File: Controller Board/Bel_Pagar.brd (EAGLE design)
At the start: 7 parts, among them IC1 7805T, Q1 BD140

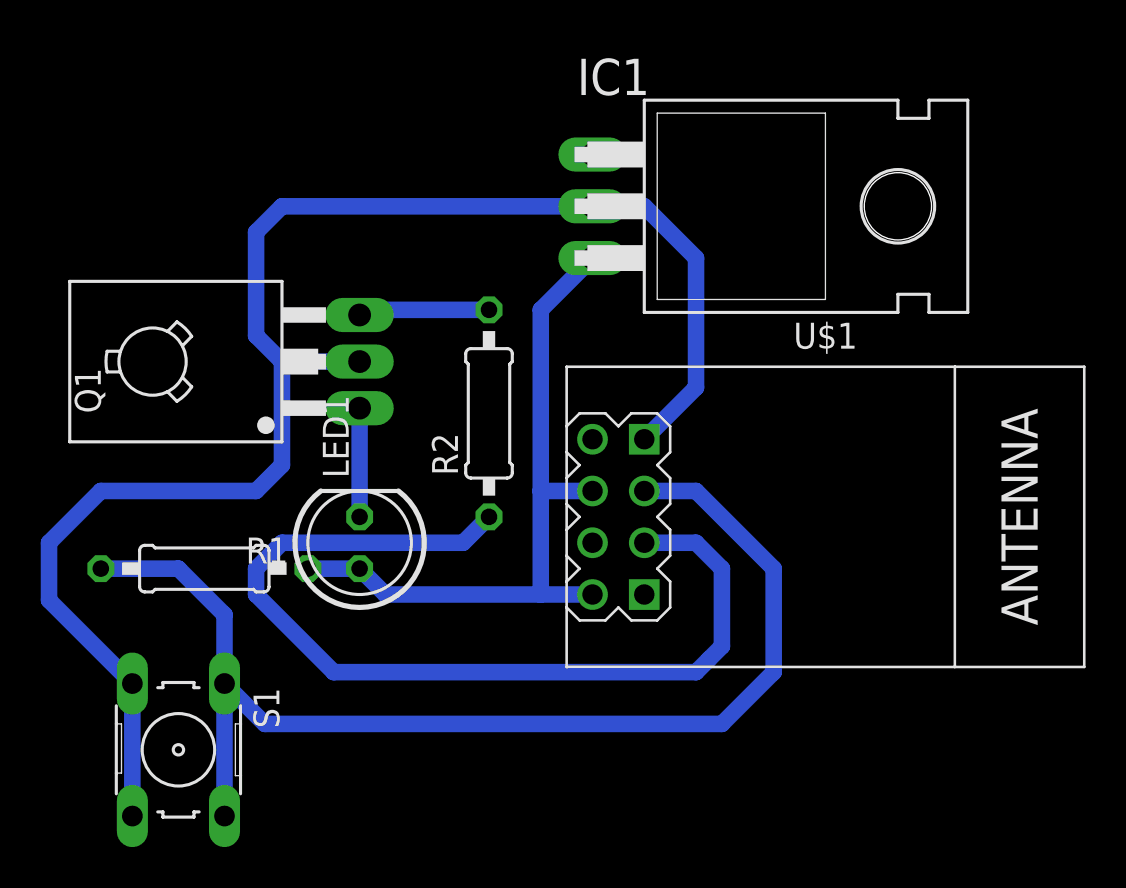
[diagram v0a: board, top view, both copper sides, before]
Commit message: Remove 7805 from controller board
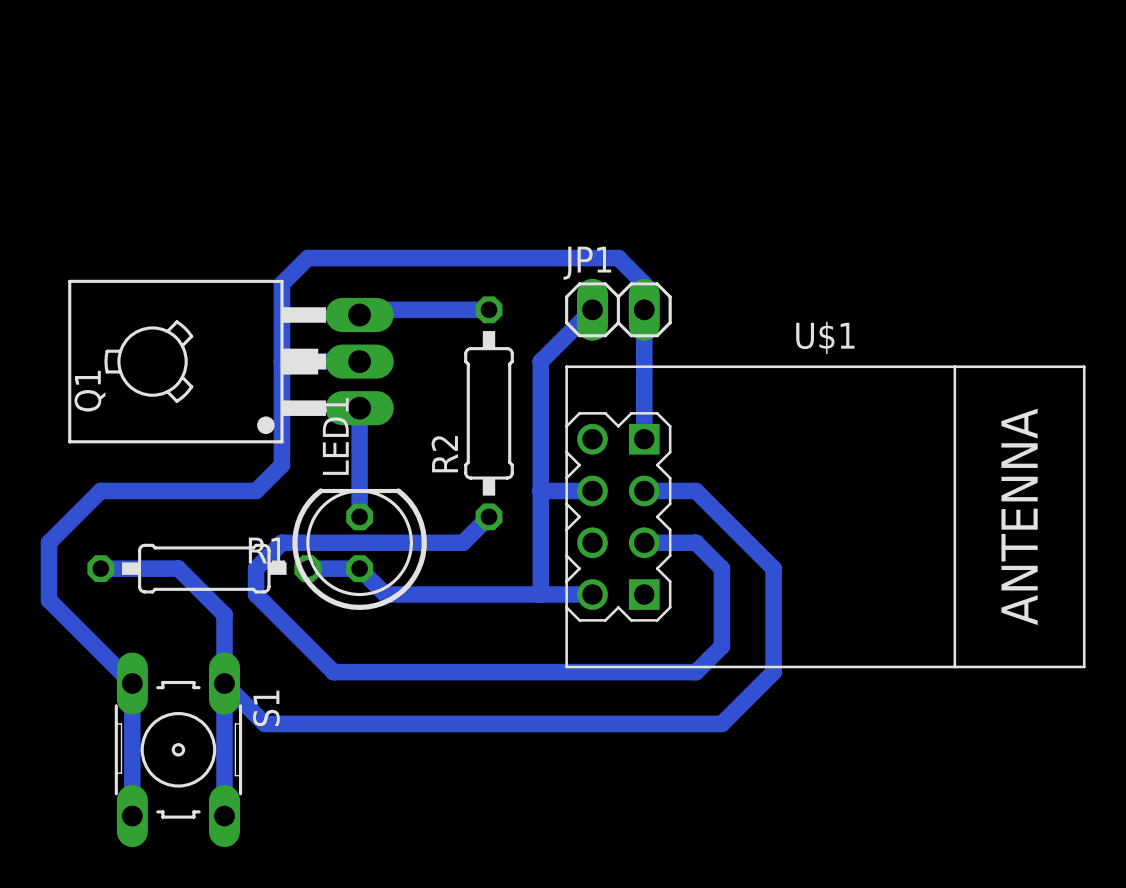
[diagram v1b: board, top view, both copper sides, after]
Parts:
- removed IC1: 7805T, linear:TO220H
- added JP1: (no value), pinhead:1X02
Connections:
- removed net VIN: IC1.1
- net GND: now also JP1.2; no longer IC1.2
- net VCC: now also JP1.1; no longer IC1.3
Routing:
- net GND: track 77.0 -> 67.3 mm
- net VCC: track 34.6 -> 32.1 mm
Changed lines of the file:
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@@
 </autorouter>
 <elements>
-<element name="IC1" library="linear" library_urn="urn:adsk.eagle:library:262" package="TO220H" package3d_urn="urn:adsk.eagle:package:16414/1" value="7805T" x="64.77" y="85.09" smashed="yes" rot="R270">
-<attribute name="NAME" x="53.848" y="90.551" size="1.778" layer="25" ratio="10"/>
-<attribute name="POPULARITY" value="35" x="52.07" y="63.5" size="1.778" layer="27" rot="R270" display="off"/>
-<attribute name="VALUE" x="53.721" y="77.724" size="1.778" layer="27" ratio="10"/>
-</element>
 <element name="LED1" library="led" library_urn="urn:adsk.eagle:library:259" package="LED5MM" package3d_urn="urn:adsk.eagle:package:15799/2" value="" x="43.18" y="68.58" smashed="yes" rot="R90">
 <attribute name="NAME" x="42.6466" y="71.755" size="1.27" layer="25" ratio="10" rot="R90"/>
@@
 <attribute name="VALUE" x="66.04" y="61.595" size="1.27" layer="27" align="top-center"/>
 </element>
+<element name="JP1" library="pinhead" library_urn="urn:adsk.eagle:library:325" package="1X02" package3d_urn="urn:adsk.eagle:package:22435/2" value="" x="55.88" y="80.01" smashed="yes">
+<attribute name="NAME" x="53.2638" y="81.8388" size="1.27" layer="25" ratio="10"/>
+<attribute name="POPULARITY" value="98" x="55.88" y="80.01" size="1.778" layer="27" display="off"/>
+<attribute name="VALUE" x="53.34" y="76.835" size="1.27" layer="27"/>
+</element>
 </elements>
 <signals>
-<signal name="VIN">
-<contactref element="IC1" pad="1"/>
-</signal>
 <signal name="GND">
-<contactref element="IC1" pad="2"/>
 <contactref element="U$1" pad="A1"/>
 <contactref element="S1" pad="4"/>
 <contactref element="S1" pad="3"/>
 <contactref element="Q1" pad="2"/>
-<wire x1="57.15" y1="73.66" x2="59.69" y2="76.2" width="0.8128" layer="16"/>
-<wire x1="59.69" y1="76.2" x2="59.69" y2="82.55" width="0.8128" layer="16"/>
-<wire x1="59.69" y1="82.55" x2="57.15" y2="85.09" width="0.8128" layer="16"/>
-<wire x1="57.15" y1="85.09" x2="54.61" y2="85.09" width="0.8128" layer="16"/>
-<wire x1="54.61" y1="85.09" x2="39.37" y2="85.09" width="0.8128" layer="16"/>
-<wire x1="39.37" y1="85.09" x2="38.1" y2="83.82" width="0.8128" layer="16"/>
-<wire x1="38.1" y1="83.82" x2="38.1" y2="78.74" width="0.8128" layer="16"/>
-<wire x1="38.1" y1="78.74" x2="39.37" y2="77.47" width="0.8128" layer="16"/>
 <wire x1="39.37" y1="77.47" x2="43.18" y2="77.47" width="0.8128" layer="16"/>
 <wire x1="32.0294" y1="55.1688" x2="32.0294" y2="61.6712" width="0.8128" layer="16"/>
@@
 <wire x1="38.1" y1="71.12" x2="39.37" y2="72.39" width="0.8128" layer="16"/>
 <wire x1="39.37" y1="72.39" x2="39.37" y2="77.47" width="0.8128" layer="16"/>
+<contactref element="JP1" pad="2"/>
+<wire x1="57.15" y1="73.66" x2="57.15" y2="80.01" width="0.8128" layer="16"/>
+<wire x1="57.15" y1="80.01" x2="57.15" y2="81.28" width="0.8128" layer="16"/>
+<wire x1="57.15" y1="81.28" x2="55.88" y2="82.55" width="0.8128" layer="16"/>
+<wire x1="55.88" y1="82.55" x2="40.64" y2="82.55" width="0.8128" layer="16"/>
+<wire x1="40.64" y1="82.55" x2="39.37" y2="81.28" width="0.8128" layer="16"/>
+<wire x1="39.37" y1="81.28" x2="39.37" y2="77.47" width="0.8128" layer="16"/>
 </signal>
 <signal name="VCC">
-<contactref element="IC1" pad="3"/>
 <contactref element="U$1" pad="D2"/>
 <contactref element="U$1" pad="B2"/>
@@
 <wire x1="44.45" y1="66.04" x2="43.18" y2="67.31" width="0.8128" layer="16"/>
 <wire x1="40.64" y1="67.31" x2="43.18" y2="67.31" width="0.8128" layer="16"/>
-<wire x1="54.61" y1="82.55" x2="52.07" y2="80.01" width="0.8128" layer="16"/>
-<wire x1="52.07" y1="80.01" x2="52.07" y2="71.12" width="0.8128" layer="16"/>
 <wire x1="52.07" y1="71.12" x2="52.07" y2="66.04" width="0.8128" layer="16"/>
 <wire x1="54.61" y1="71.12" x2="52.07" y2="71.12" width="0.8128" layer="16"/>
+<contactref element="JP1" pad="1"/>
+<wire x1="54.61" y1="80.01" x2="52.07" y2="77.47" width="0.8128" layer="16"/>
+<wire x1="52.07" y1="77.47" x2="52.07" y2="71.12" width="0.8128" layer="16"/>
 </signal>
 <signal name="BELL">
